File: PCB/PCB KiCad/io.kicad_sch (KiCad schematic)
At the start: 0 parts

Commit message: draw schematic for 60%
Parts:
- added D? (x2): LED, symbol Device:LED
- added SW? (x2): SW_Push, symbol Switch:SW_Push
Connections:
- new net +3V3: D?.2 (A)
- new net GND: D?.1 (K), D?.1 (K), SW?.1, SW?.1
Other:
- note added: "Buttons"
- note added: "Connectors"
- note added: "LEDs"
- note added: "TO DO: QWIIC Logic points Button connectos Nets"
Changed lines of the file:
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@@
 (kicad_sch (version 20211123) (generator eeschema)
   (paper "A4")
+  (wire (pts (xy 176.53 43.18) (xy 176.53 53.34))
+    (stroke (width 0) (type default) (color 0 0 0 0))
+  )
+  (wire (pts (xy 176.53 63.5) (xy 176.53 69.85))
+    (stroke (width 0) (type default) (color 0 0 0 0))
+  )
+  (wire (pts (xy 60.96 40.64) (xy 60.96 49.53))
+    (stroke (width 0) (type default) (color 0 0 0 0))
+  )
+  (wire (pts (xy 200.66 63.5) (xy 200.66 69.85))
+    (stroke (width 0) (type default) (color 0 0 0 0))
+  )
+  (wire (pts (xy 45.72 57.15) (xy 45.72 63.5))
+    (stroke (width 0) (type default) (color 0 0 0 0))
+  )
+  (wire (pts (xy 45.72 41.91) (xy 45.72 49.53))
+    (stroke (width 0) (type default) (color 0 0 0 0))
+  )
+  (wire (pts (xy 60.96 57.15) (xy 60.96 63.5))
+    (stroke (width 0) (type default) (color 0 0 0 0))
+  )
+  (wire (pts (xy 200.66 43.18) (xy 200.66 53.34))
+    (stroke (width 0) (type default) (color 0 0 0 0))
+  )
+  (text "Connectors" (at 172.72 113.03 0)
+    (effects (font (size 3 3)) (justify left bottom))
+  )
+  (text "TO DO:\nQWIIC\nLogic points\nButton connectos\nNets\n" (at 186.69 127 0)
+    (effects (font (size 1.5 1.5)) (justify left bottom))
+  )
+  (text "Buttons" (at 173.99 31.75 0)
+    (effects (font (size 3 3)) (justify left bottom))
+  )
+  (text "LEDs" (at 35.56 29.21 0)
+    (effects (font (size 3 3)) (justify left bottom))
+  )
+  (symbol (lib_id "Device:LED") (at 60.96 53.34 90) (unit 1)
+    (in_bom yes) (on_board yes) (fields_autoplaced)
+    (property "Reference" "D?" (id 0) (at 64.77 53.6574 90)
+      (effects (font (size 1.27 1.27)) (justify right))
+    )
+    (property "Value" "LED" (id 1) (at 64.77 56.1974 90)
+      (effects (font (size 1.27 1.27)) (justify right))
+    )
+    (property "Footprint" "" (id 2) (at 60.96 53.34 0)
+      (effects (font (size 1.27 1.27)) hide)
+    )
+    (property "Datasheet" "~" (id 3) (at 60.96 53.34 0)
+      (effects (font (size 1.27 1.27)) hide)
+    )
+    (pin "1")
+    (pin "2")
+  )
+  (symbol (lib_id "power:GND") (at 200.66 69.85 0) (unit 1)
+    (in_bom yes) (on_board yes) (fields_autoplaced)
+    (property "Reference" "#PWR?" (id 0) (at 200.66 76.2 0)
+      (effects (font (size 1.27 1.27)) hide)
+    )
+    (property "Value" "GND" (id 1) (at 200.66 74.93 0))
+    (property "Footprint" "" (id 2) (at 200.66 69.85 0)
+      (effects (font (size 1.27 1.27)) hide)
+    )
+    (property "Datasheet" "" (id 3) (at 200.66 69.85 0)
+      (effects (font (size 1.27 1.27)) hide)
+    )
+    (pin "1")
+  )
+  (symbol (lib_id "Switch:SW_Push") (at 200.66 58.42 90) (unit 1)
+    (in_bom yes) (on_board yes) (fields_autoplaced)
+    (property "Reference" "SW?" (id 0) (at 201.93 57.1499 90)
+      (effects (font (size 1.27 1.27)) (justify right))
+    )
+    (property "Value" "SW_Push" (id 1) (at 201.93 59.6899 90)
+      (effects (font (size 1.27 1.27)) (justify right))
+    )
+    (property "Footprint" "" (id 2) (at 195.58 58.42 0)
+      (effects (font (size 1.27 1.27)) hide)
+    )
+    (property "Datasheet" "~" (id 3) (at 195.58 58.42 0)
+      (effects (font (size 1.27 1.27)) hide)
+    )
+    (pin "1")
+    (pin "2")
+  )
+  (symbol (lib_id "power:+3.3V") (at 45.72 41.91 0) (unit 1)
+    (in_bom yes) (on_board yes) (fields_autoplaced)
+    (property "Reference" "#PWR?" (id 0) (at 45.72 45.72 0)
+      (effects (font (size 1.27 1.27)) hide)
+    )
+    (property "Value" "+3.3V" (id 1) (at 45.72 36.83 0))
+    (property "Footprint" "" (id 2) (at 45.72 41.91 0)
+      (effects (font (size 1.27 1.27)) hide)
+    )
+    (property "Datasheet" "" (id 3) (at 45.72 41.91 0)
+      (effects (font (size 1.27 1.27)) hide)
+    )
+    (pin "1")
+  )
+  (symbol (lib_id "Device:LED") (at 45.72 53.34 90) (unit 1)
+    (in_bom yes) (on_board yes) (fields_autoplaced)
+    (property "Reference" "D?" (id 0) (at 49.53 53.6574 90)
+      (effects (font (size 1.27 1.27)) (justify right))
+    )
+    (property "Value" "LED" (id 1) (at 49.53 56.1974 90)
+      (effects (font (size 1.27 1.27)) (justify right))
+    )
+    (property "Footprint" "" (id 2) (at 45.72 53.34 0)
+      (effects (font (size 1.27 1.27)) hide)
+    )
+    (property "Datasheet" "~" (id 3) (at 45.72 53.34 0)
+      (effects (font (size 1.27 1.27)) hide)
+    )
+    (pin "1")
+    (pin "2")
+  )
+  (symbol (lib_id "power:GND") (at 176.53 69.85 0) (unit 1)
+    (in_bom yes) (on_board yes) (fields_autoplaced)
+    (property "Reference" "#PWR?" (id 0) (at 176.53 76.2 0)
+      (effects (font (size 1.27 1.27)) hide)
+    )
+    (property "Value" "GND" (id 1) (at 176.53 74.93 0))
+    (property "Footprint" "" (id 2) (at 176.53 69.85 0)
+      (effects (font (size 1.27 1.27)) hide)
+    )
+    (property "Datasheet" "" (id 3) (at 176.53 69.85 0)
+      (effects (font (size 1.27 1.27)) hide)
+    )
+    (pin "1")
+  )
+  (symbol (lib_id "power:GND") (at 60.96 63.5 0) (unit 1)
+    (in_bom yes) (on_board yes) (fields_autoplaced)
+    (property "Reference" "#PWR?" (id 0) (at 60.96 69.85 0)
+      (effects (font (size 1.27 1.27)) hide)
+    )
+    (property "Value" "GND" (id 1) (at 60.96 68.58 0))
+    (property "Footprint" "" (id 2) (at 60.96 63.5 0)
+      (effects (font (size 1.27 1.27)) hide)
+    )
+    (property "Datasheet" "" (id 3) (at 60.96 63.5 0)
+      (effects (font (size 1.27 1.27)) hide)
+    )
+    (pin "1")
+  )
+  (symbol (lib_id "power:GND") (at 45.72 63.5 0) (unit 1)
+    (in_bom yes) (on_board yes) (fields_autoplaced)
+    (property "Reference" "#PWR?" (id 0) (at 45.72 69.85 0)
+      (effects (font (size 1.27 1.27)) hide)
+    )
+    (property "Value" "GND" (id 1) (at 45.72 68.58 0))
+    (property "Footprint" "" (id 2) (at 45.72 63.5 0)
+      (effects (font (size 1.27 1.27)) hide)
+    )
+    (property "Datasheet" "" (id 3) (at 45.72 63.5 0)
+      (effects (font (size 1.27 1.27)) hide)
+    )
+    (pin "1")
+  )
+  (symbol (lib_id "Switch:SW_Push") (at 176.53 58.42 90) (unit 1)
+    (in_bom yes) (on_board yes) (fields_autoplaced)
+    (property "Reference" "SW?" (id 0) (at 177.8 57.1499 90)
+      (effects (font (size 1.27 1.27)) (justify right))
+    )
+    (property "Value" "SW_Push" (id 1) (at 177.8 59.6899 90)
+      (effects (font (size 1.27 1.27)) (justify right))
+    )
+    (property "Footprint" "" (id 2) (at 171.45 58.42 0)
+      (effects (font (size 1.27 1.27)) hide)
+    )
+    (property "Datasheet" "~" (id 3) (at 171.45 58.42 0)
+      (effects (font (size 1.27 1.27)) hide)
+    )
+    (pin "1")
+    (pin "2")
+  )
 )

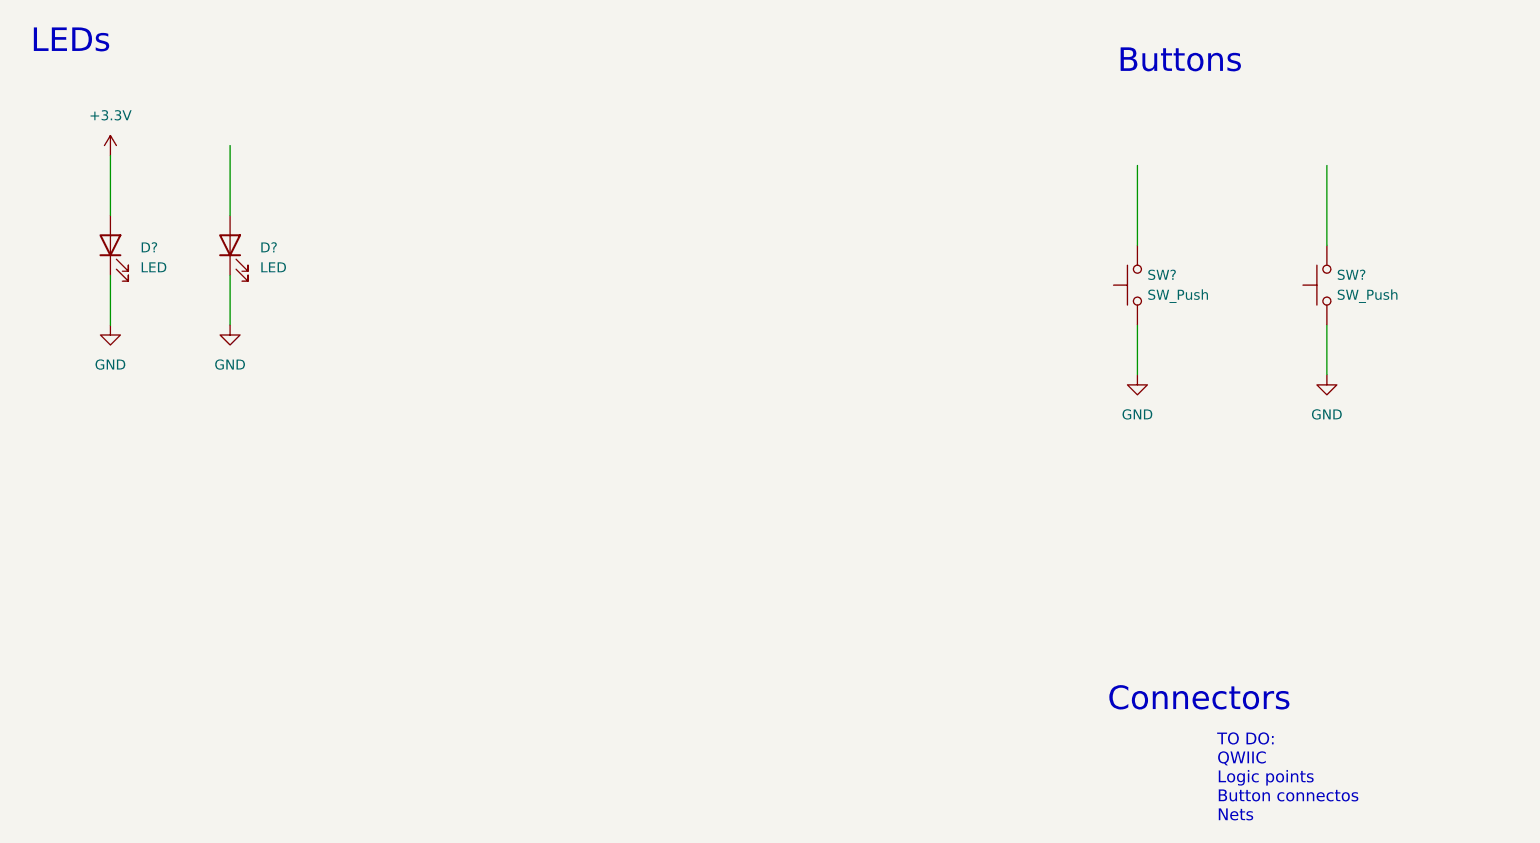
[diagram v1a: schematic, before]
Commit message: Add buttons: MCU RESET, TRIGGER
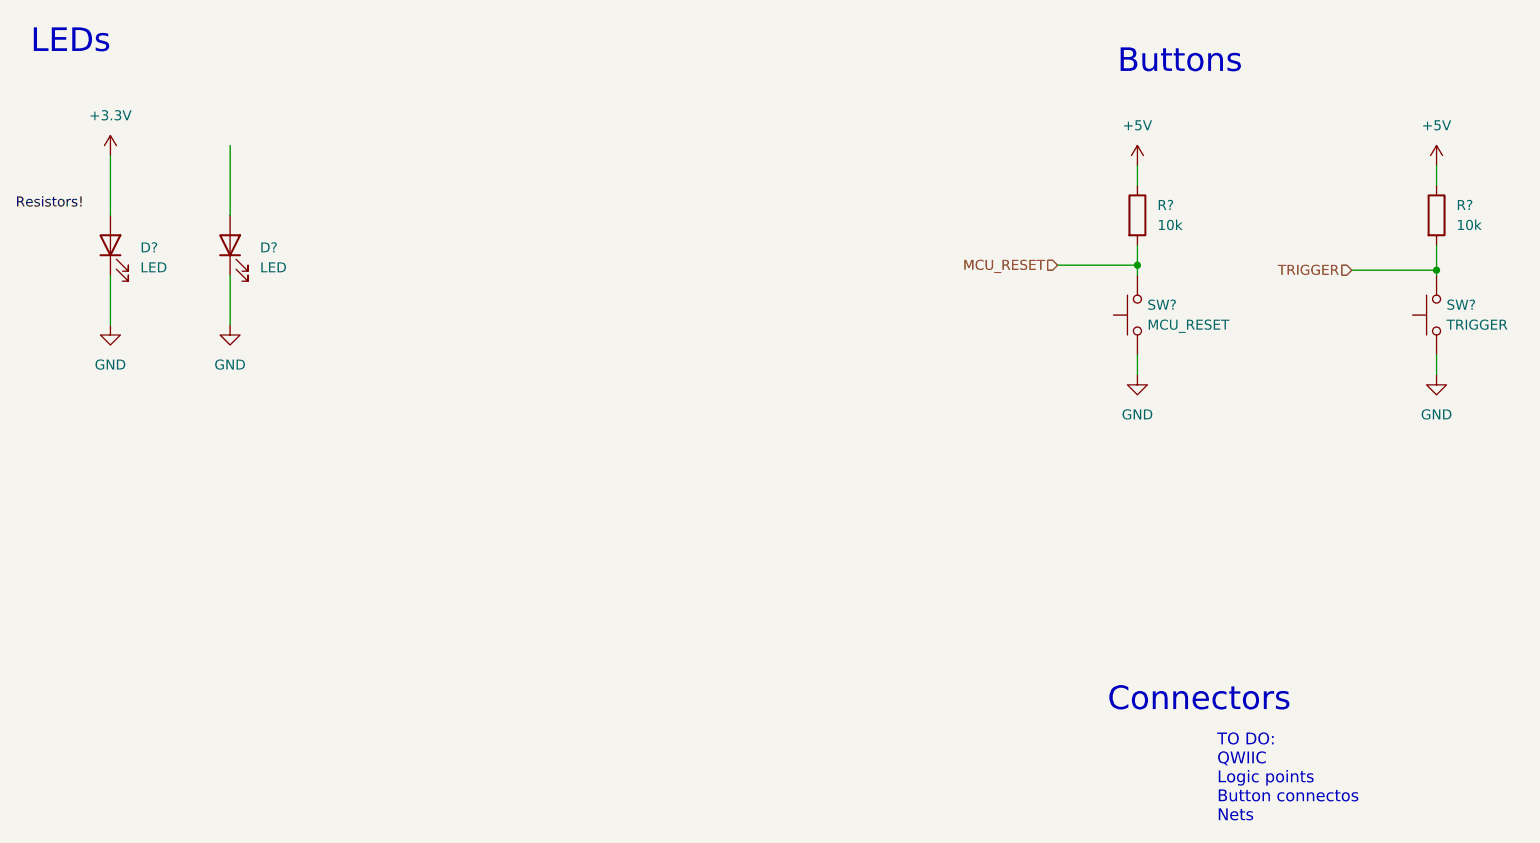
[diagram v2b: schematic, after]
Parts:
- added R? (x2): 10k, symbol Device:R
- SW?: value SW_Push -> TRIGGER
- SW?: value SW_Push -> MCU_RESET
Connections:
- net TRIGGER: now reaches SW?.2
- net TRIGGER: now also R?.2
- net MCU_RESET: now reaches SW?.2
- net MCU_RESET: now also R?.2
- new net +5V: R?.1, R?.1
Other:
- moved on the sheet: SW?
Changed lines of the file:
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@@
 (kicad_sch (version 20211123) (generator eeschema)
   (paper "A4")
-  (wire (pts (xy 176.53 43.18) (xy 176.53 53.34))
-    (stroke (width 0) (type default) (color 0 0 0 0))
-  )
-  (wire (pts (xy 176.53 63.5) (xy 176.53 69.85))
+  (junction (at 176.53 55.88) (diameter 0) (color 0 0 0 0)
+  )
+  (junction (at 214.63 56.515) (diameter 0) (color 0 0 0 0)
+  )
+  (wire (pts (xy 176.53 55.88) (xy 176.53 57.15))
+    (stroke (width 0) (type default) (color 0 0 0 0))
+  )
+  (wire (pts (xy 214.63 53.34) (xy 214.63 56.515))
+    (stroke (width 0) (type default) (color 0 0 0 0))
+  )
+  (wire (pts (xy 176.53 43.18) (xy 176.53 45.72))
+    (stroke (width 0) (type default) (color 0 0 0 0))
+  )
+  (wire (pts (xy 203.835 56.515) (xy 214.63 56.515))
+    (stroke (width 0) (type default) (color 0 0 0 0))
+  )
+  (wire (pts (xy 176.53 67.31) (xy 176.53 69.85))
     (stroke (width 0) (type default) (color 0 0 0 0))
   )
@@
     (stroke (width 0) (type default) (color 0 0 0 0))
   )
-  (wire (pts (xy 200.66 63.5) (xy 200.66 69.85))
+  (wire (pts (xy 214.63 67.31) (xy 214.63 69.85))
+    (stroke (width 0) (type default) (color 0 0 0 0))
+  )
+  (wire (pts (xy 176.53 53.34) (xy 176.53 55.88))
     (stroke (width 0) (type default) (color 0 0 0 0))
   )
@@
     (stroke (width 0) (type default) (color 0 0 0 0))
   )
+  (wire (pts (xy 166.37 55.88) (xy 176.53 55.88))
+    (stroke (width 0) (type default) (color 0 0 0 0))
+  )
   (wire (pts (xy 60.96 57.15) (xy 60.96 63.5))
     (stroke (width 0) (type default) (color 0 0 0 0))
   )
-  (wire (pts (xy 200.66 43.18) (xy 200.66 53.34))
+  (wire (pts (xy 214.63 56.515) (xy 214.63 57.15))
+    (stroke (width 0) (type default) (color 0 0 0 0))
+  )
+  (wire (pts (xy 214.63 43.18) (xy 214.63 45.72))
     (stroke (width 0) (type default) (color 0 0 0 0))
   )
@@
     (effects (font (size 3 3)) (justify left bottom))
   )
+  (label "Resistors!" (at 33.655 48.895 0)
+    (effects (font (size 1.27 1.27)) (justify left bottom))
+  )
+  (hierarchical_label "MCU_RESET" (shape input) (at 166.37 55.88 180)
+    (effects (font (size 1.27 1.27)) (justify right))
+  )
+  (hierarchical_label "TRIGGER" (shape input) (at 203.835 56.515 180)
+    (effects (font (size 1.27 1.27)) (justify right))
+  )
   (symbol (lib_id "Device:LED") (at 60.96 53.34 90) (unit 1)
     (in_bom yes) (on_board yes) (fields_autoplaced)
@@
     (pin "2")
   )
-  (symbol (lib_id "power:GND") (at 200.66 69.85 0) (unit 1)
-    (in_bom yes) (on_board yes) (fields_autoplaced)
-    (property "Reference" "#PWR?" (id 0) (at 200.66 76.2 0)
-      (effects (font (size 1.27 1.27)) hide)
-    )
-    (property "Value" "GND" (id 1) (at 200.66 74.93 0))
-    (property "Footprint" "" (id 2) (at 200.66 69.85 0)
-      (effects (font (size 1.27 1.27)) hide)
-    )
-    (property "Datasheet" "" (id 3) (at 200.66 69.85 0)
-      (effects (font (size 1.27 1.27)) hide)
-    )
-    (pin "1")
-  )
-  (symbol (lib_id "Switch:SW_Push") (at 200.66 58.42 90) (unit 1)
-    (in_bom yes) (on_board yes) (fields_autoplaced)
-    (property "Reference" "SW?" (id 0) (at 201.93 57.1499 90)
-      (effects (font (size 1.27 1.27)) (justify right))
-    )
-    (property "Value" "SW_Push" (id 1) (at 201.93 59.6899 90)
-      (effects (font (size 1.27 1.27)) (justify right))
-    )
-    (property "Footprint" "" (id 2) (at 195.58 58.42 0)
-      (effects (font (size 1.27 1.27)) hide)
-    )
-    (property "Datasheet" "~" (id 3) (at 195.58 58.42 0)
+  (symbol (lib_id "Device:R") (at 176.53 49.53 0) (unit 1)
+    (in_bom yes) (on_board yes) (fields_autoplaced)
+    (property "Reference" "R?" (id 0) (at 179.07 48.2599 0)
+      (effects (font (size 1.27 1.27)) (justify left))
+    )
+    (property "Value" "10k" (id 1) (at 179.07 50.7999 0)
+      (effects (font (size 1.27 1.27)) (justify left))
+    )
+    (property "Footprint" "" (id 2) (at 174.752 49.53 90)
+      (effects (font (size 1.27 1.27)) hide)
+    )
+    (property "Datasheet" "~" (id 3) (at 176.53 49.53 0)
+      (effects (font (size 1.27 1.27)) hide)
+    )
+    (pin "1")
+    (pin "2")
+  )
+  (symbol (lib_id "power:+5V") (at 176.53 43.18 0) (unit 1)
+    (in_bom yes) (on_board yes) (fields_autoplaced)
+    (property "Reference" "#PWR?" (id 0) (at 176.53 46.99 0)
+      (effects (font (size 1.27 1.27)) hide)
+    )
+    (property "Value" "+5V" (id 1) (at 176.53 38.1 0))
+    (property "Footprint" "" (id 2) (at 176.53 43.18 0)
+      (effects (font (size 1.27 1.27)) hide)
+    )
+    (property "Datasheet" "" (id 3) (at 176.53 43.18 0)
+      (effects (font (size 1.27 1.27)) hide)
+    )
+    (pin "1")
+  )
+  (symbol (lib_id "power:GND") (at 214.63 69.85 0) (unit 1)
+    (in_bom yes) (on_board yes) (fields_autoplaced)
+    (property "Reference" "#PWR?" (id 0) (at 214.63 76.2 0)
+      (effects (font (size 1.27 1.27)) hide)
+    )
+    (property "Value" "GND" (id 1) (at 214.63 74.93 0))
+    (property "Footprint" "" (id 2) (at 214.63 69.85 0)
+      (effects (font (size 1.27 1.27)) hide)
+    )
+    (property "Datasheet" "" (id 3) (at 214.63 69.85 0)
+      (effects (font (size 1.27 1.27)) hide)
+    )
+    (pin "1")
+  )
+  (symbol (lib_id "Switch:SW_Push") (at 214.63 62.23 90) (unit 1)
+    (in_bom yes) (on_board yes) (fields_autoplaced)
+    (property "Reference" "SW?" (id 0) (at 215.9 60.9599 90)
+      (effects (font (size 1.27 1.27)) (justify right))
+    )
+    (property "Value" "TRIGGER" (id 1) (at 215.9 63.4999 90)
+      (effects (font (size 1.27 1.27)) (justify right))
+    )
+    (property "Footprint" "" (id 2) (at 209.55 62.23 0)
+      (effects (font (size 1.27 1.27)) hide)
+    )
+    (property "Datasheet" "~" (id 3) (at 209.55 62.23 0)
+      (effects (font (size 1.27 1.27)) hide)
+    )
+    (pin "1")
+    (pin "2")
+  )
+  (symbol (lib_id "Device:R") (at 214.63 49.53 0) (unit 1)
+    (in_bom yes) (on_board yes) (fields_autoplaced)
+    (property "Reference" "R?" (id 0) (at 217.17 48.2599 0)
+      (effects (font (size 1.27 1.27)) (justify left))
+    )
+    (property "Value" "10k" (id 1) (at 217.17 50.7999 0)
+      (effects (font (size 1.27 1.27)) (justify left))
+    )
+    (property "Footprint" "" (id 2) (at 212.852 49.53 90)
+      (effects (font (size 1.27 1.27)) hide)
+    )
+    (property "Datasheet" "~" (id 3) (at 214.63 49.53 0)
       (effects (font (size 1.27 1.27)) hide)
     )
@@
     (pin "1")
   )
+  (symbol (lib_id "power:+5V") (at 214.63 43.18 0) (unit 1)
+    (in_bom yes) (on_board yes) (fields_autoplaced)
+    (property "Reference" "#PWR?" (id 0) (at 214.63 46.99 0)
+      (effects (font (size 1.27 1.27)) hide)
+    )
+    (property "Value" "+5V" (id 1) (at 214.63 38.1 0))
+    (property "Footprint" "" (id 2) (at 214.63 43.18 0)
+      (effects (font (size 1.27 1.27)) hide)
+    )
+    (property "Datasheet" "" (id 3) (at 214.63 43.18 0)
+      (effects (font (size 1.27 1.27)) hide)
+    )
+    (pin "1")
+  )
   (symbol (lib_id "Device:LED") (at 45.72 53.34 90) (unit 1)
     (in_bom yes) (on_board yes) (fields_autoplaced)
@@
     (pin "1")
   )
-  (symbol (lib_id "Switch:SW_Push") (at 176.53 58.42 90) (unit 1)
-    (in_bom yes) (on_board yes) (fields_autoplaced)
-    (property "Reference" "SW?" (id 0) (at 177.8 57.1499 90)
-      (effects (font (size 1.27 1.27)) (justify right))
-    )
-    (property "Value" "SW_Push" (id 1) (at 177.8 59.6899 90)
-      (effects (font (size 1.27 1.27)) (justify right))
-    )
-    (property "Footprint" "" (id 2) (at 171.45 58.42 0)
-      (effects (font (size 1.27 1.27)) hide)
-    )
-    (property "Datasheet" "~" (id 3) (at 171.45 58.42 0)
-      (effects (font (size 1.27 1.27)) hide)
-    )
+  (symbol (lib_id "Switch:SW_Push") (at 176.53 62.23 90) (unit 1)
+    (in_bom yes) (on_board yes) (fields_autoplaced)
+    (property "Reference" "SW?" (id 0) (at 177.8 60.9599 90)
+      (effects (font (size 1.27 1.27)) (justify right))
+    )
+    (property "Value" "MCU_RESET" (id 1) (at 177.8 63.4999 90)
+      (effects (font (size 1.27 1.27)) (justify right))
+    )
+    (property "Footprint" "" (id 2) (at 171.45 62.23 0)
+      (effects (font (size 1.27 1.27)) hide)
+    )
+    (property "Datasheet" "~" (id 3) (at 171.45 62.23 0)
+      (effects (font (size 1.27 1.27)) hide)
+    )
